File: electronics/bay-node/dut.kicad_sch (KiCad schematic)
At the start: 24 parts, among them J5 AUX, Q2 2N7002, Q3 2N7002, U10 INA226AIDGSR, U9 TPS2553DBVR

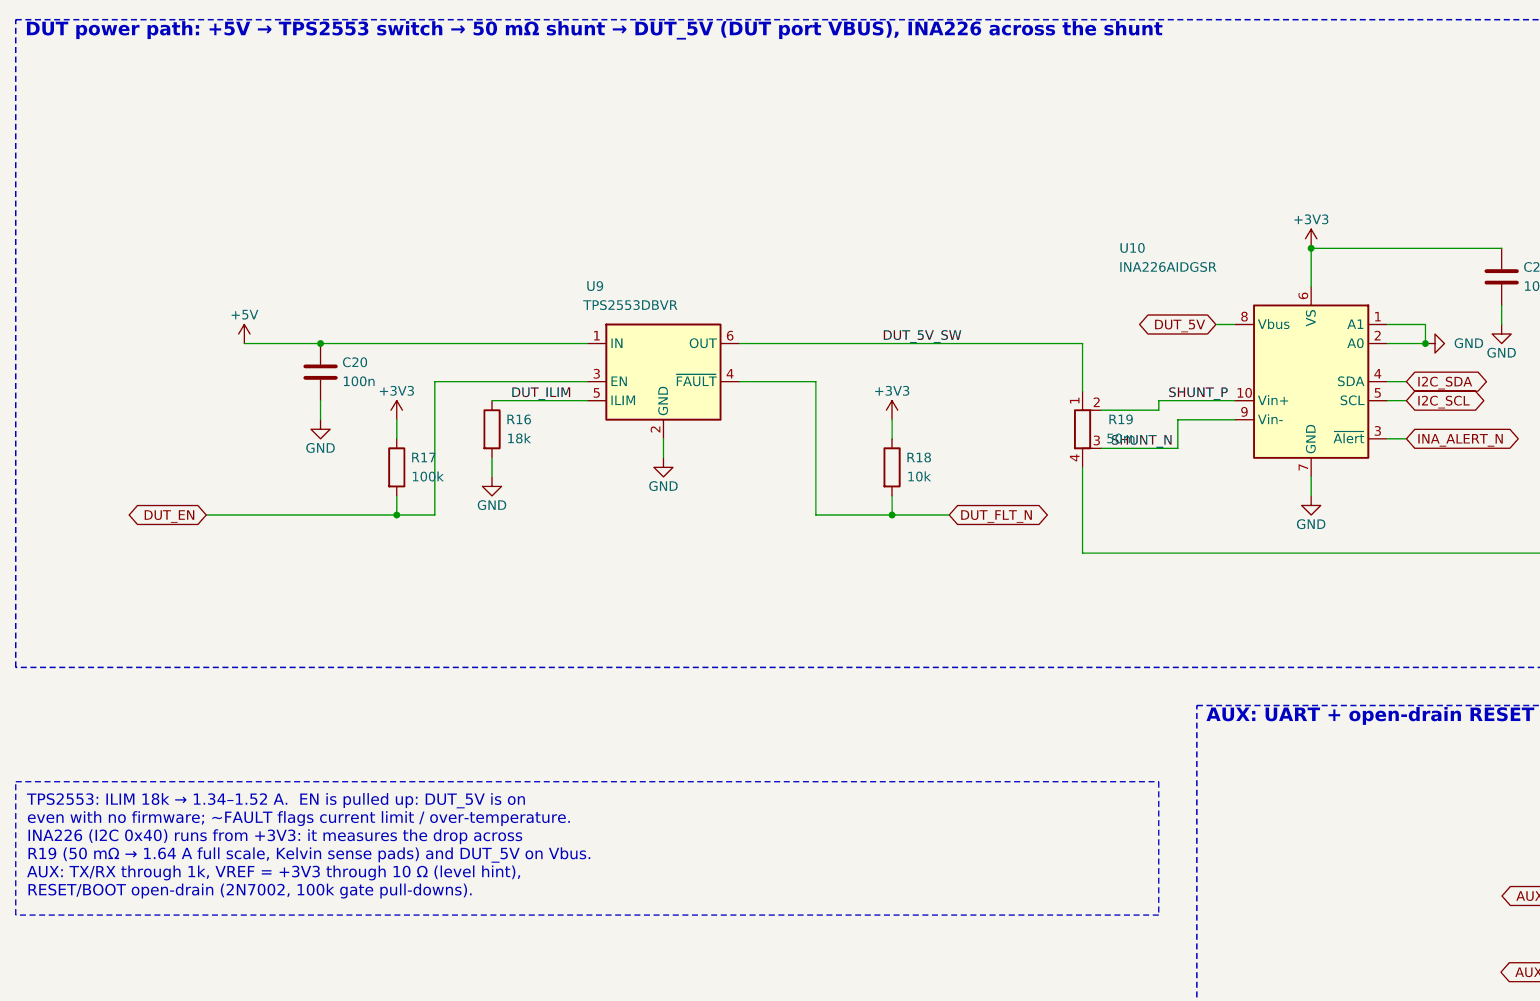
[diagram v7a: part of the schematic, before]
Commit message: Bay node 74 × 90: no J4, AUX and DATA side entry on the right edge
The node grows 10 mm on the right and drops the DUT receptacle J4 (the
user's option B, 2026-10-19): every DUT hangs on the DATA lead.

- J7 (DATA, S8B) and J5 (AUX, S6B) are side entry on the right edge,
  facing the drag chain; J6 (CAM) stays vertical at the rear right, its
  lead straight back, east of the antenna keep-out.  J2 and the right
  holes (x 70.5) move to the new edge; the front half and the left holes
  stay (the tray's access holes, a09923f).
- U8 is the last part before J7; the hand-drawn HS chain ends on J7's
  pads (DUT_CONN matched with its two vias).  R14/R15 go with J4.
- +5V at 5.24 V (FB 100k/18k) for the DATA board at 1.4 A; INA226 Vbus
  on Vin- at its pins.
- Docs: electronics, cabling, assembly, power (no batteries on rack
  DUTs), the third Konnect round; BOM and JLC estimate (≈ $328), web
  scene's DATA plug, notice NODE_DATA.

Co-Authored-By: Claude Opus 5.5 <noreply@anthropic.com>
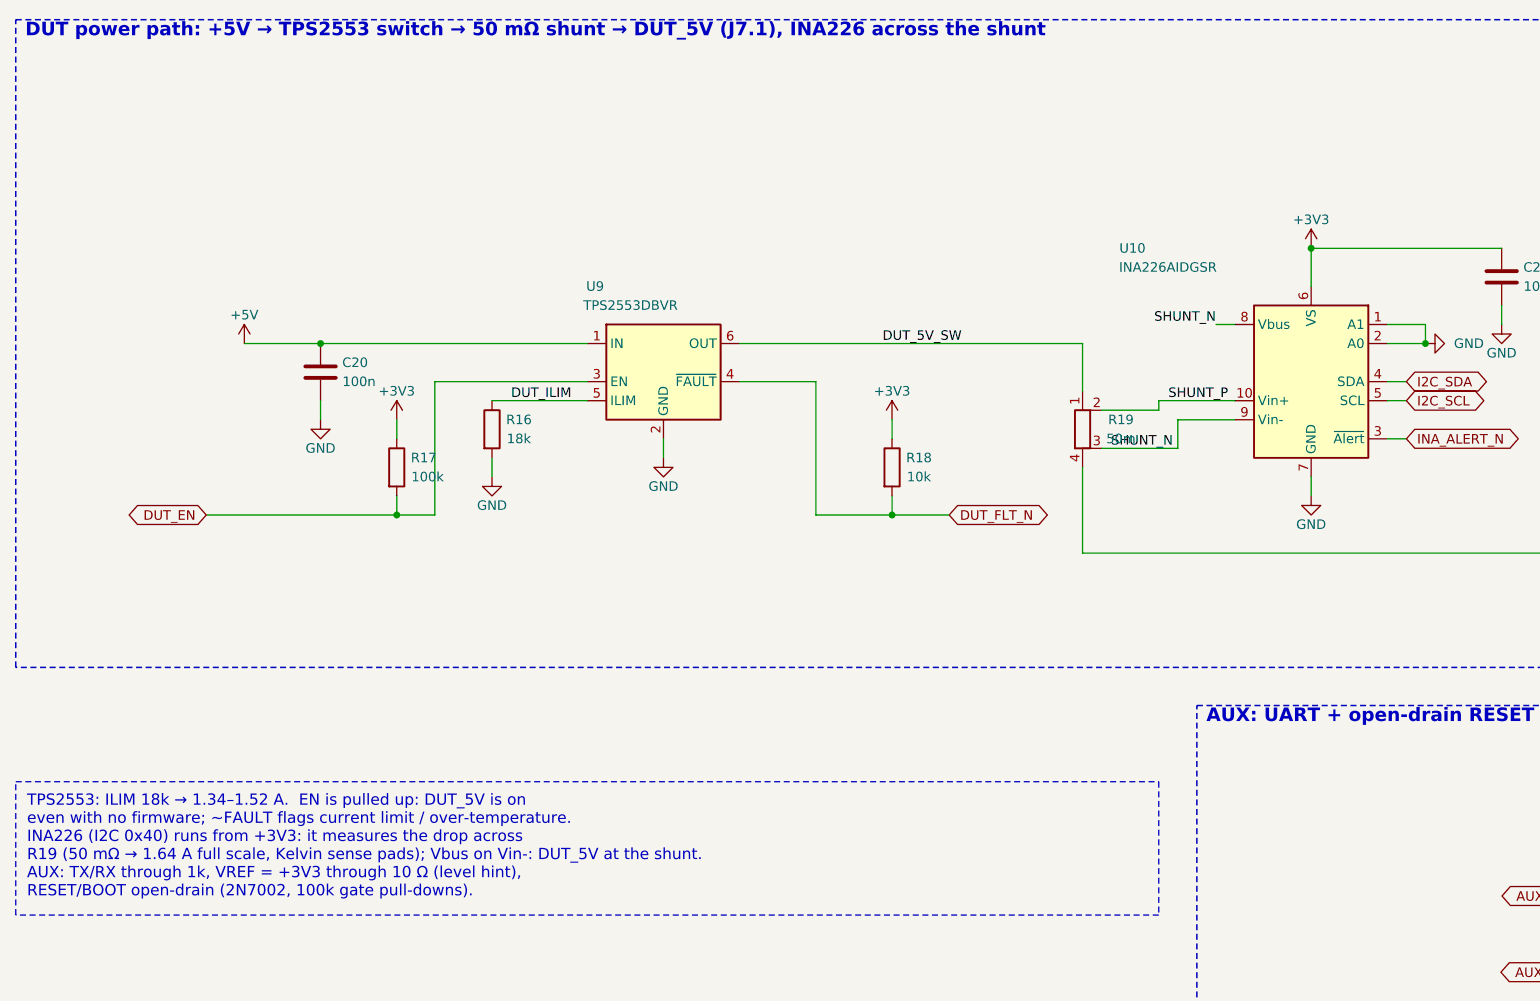
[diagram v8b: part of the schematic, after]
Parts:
- J5: footprint Connector_JST:JST_PH_B6B-PH-SM4-TB_1x06-1MP_P2.00mm_Vertical -> Connector_JST:JST_PH_S6B-PH-SM4-TB_1x06-1MP_P2.00mm_Horizontal; LCSC C471518 -> C265405; MPN B6B-PH-SM4-TB(LF)(SN) -> S6B-PH-SM4-TB(LF)(SN)
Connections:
- net DUT_5V: no longer U10.8 (Vbus)
- net SHUNT_N: now also U10.8 (Vbus)
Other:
- note added: "DUT power path: +5V → TPS2553 switch → 50 mΩ shunt → DUT_5V (J7.1), INA226 across the shunt"
- note removed: "DUT power path: +5V → TPS2553 switch → 50 mΩ shunt → DUT_5V (DUT port VBUS), INA226 across the shunt"
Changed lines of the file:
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@@
 		)
 	)
-	(global_label "DUT_5V"
-		(shape bidirectional)
+	(label "SHUNT_N"
 		(at 175.26 71.12 180)
 		(fields_autoplaced yes)
@@
 				(size 1.27 1.27)
 			)
-			(justify right)
-		)
-		(property "Intersheetrefs" "${INTERSHEET_REFS}"
-			(at 175.26 71.12 0)
-			(effects
-				(font
-					(size 1.27 1.27)
-				)
-				(justify right)
-				(hide yes)
-			)
+			(justify right bottom)
 		)
 	)
@@
 			)
 		)
-		(property "Footprint" "Connector_JST:JST_PH_B6B-PH-SM4-TB_1x06-1MP_P2.00mm_Vertical"
+		(property "Footprint" "Connector_JST:JST_PH_S6B-PH-SM4-TB_1x06-1MP_P2.00mm_Horizontal"
 			(at 269.24 162.56 0)
 			(effects
@@
 			)
 		)
-		(property "Description" "JST PH 6-pin, vertical, SMD"
+		(property "Description" "JST PH 6-pin, side entry, SMD"
 			(at 269.24 162.56 0)
 			(effects
@@
 			)
 		)
-		(property "MPN" "B6B-PH-SM4-TB(LF)(SN)"
+		(property "MPN" "S6B-PH-SM4-TB(LF)(SN)"
 			(at 269.24 162.56 0)
 			(effects
@@
 			)
 		)
-		(property "LCSC" "C471518"
+		(property "LCSC" "C265405"
 			(at 269.24 162.56 0)
 			(effects
@@
 		)
 	)
-	(text "DUT power path: +5V → TPS2553 switch → 50 mΩ shunt → DUT_5V (DUT port VBUS), INA226 across the shunt"
+	(text "DUT power path: +5V → TPS2553 switch → 50 mΩ shunt → DUT_5V (J7.1), INA226 across the shunt"
 		(exclude_from_sim no)
 		(at 16.51 33.02 0)
@@
 		)
 	)
-	(text_box "TPS2553: ILIM 18k → 1.34–1.52 A.  EN is pulled up: DUT_5V is on\n  even with no firmware; ~FAULT flags current limit / over-temperature.\nINA226 (I2C 0x40) runs from +3V3: it measures the drop across\n  R19 (50 mΩ → 1.64 A full scale, Kelvin sense pads) and DUT_5V on Vbus.\nAUX: TX/RX through 1k, VREF = +3V3 through 10 Ω (level hint),\n  RESET/BOOT open-drain (2N7002, 100k gate pull-downs)."
+	(text_box "TPS2553: ILIM 18k → 1.34–1.52 A.  EN is pulled up: DUT_5V is on\n  even with no firmware; ~FAULT flags current limit / over-temperature.\nINA226 (I2C 0x40) runs from +3V3: it measures the drop across\n  R19 (50 mΩ → 1.64 A full scale, Kelvin sense pads); Vbus on Vin-: DUT_5V at the shunt.\nAUX: TX/RX through 1k, VREF = +3V3 through 10 Ω (level hint),\n  RESET/BOOT open-drain (2N7002, 100k gate pull-downs)."
 		(exclude_from_sim no)
 		(at 15.24 132.08 0)
